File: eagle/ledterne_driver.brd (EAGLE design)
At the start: 24.3 x 23.1 mm, 9 parts, among them IC1 MEGA8-AI

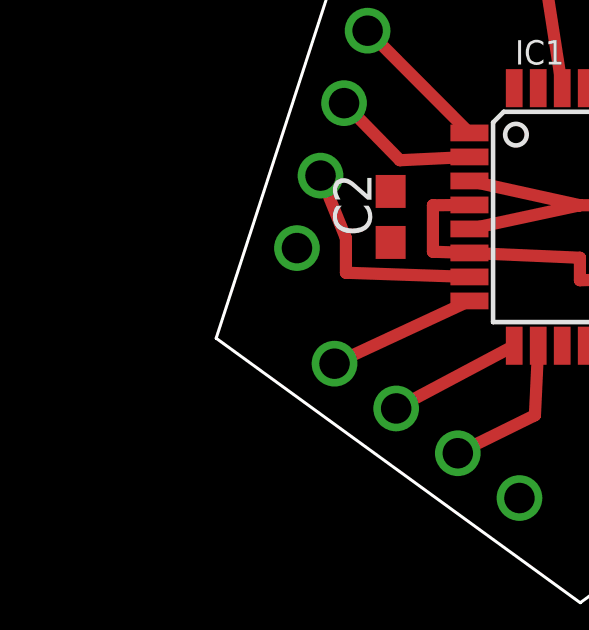
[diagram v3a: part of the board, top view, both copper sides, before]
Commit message: Add connector for supply voltage
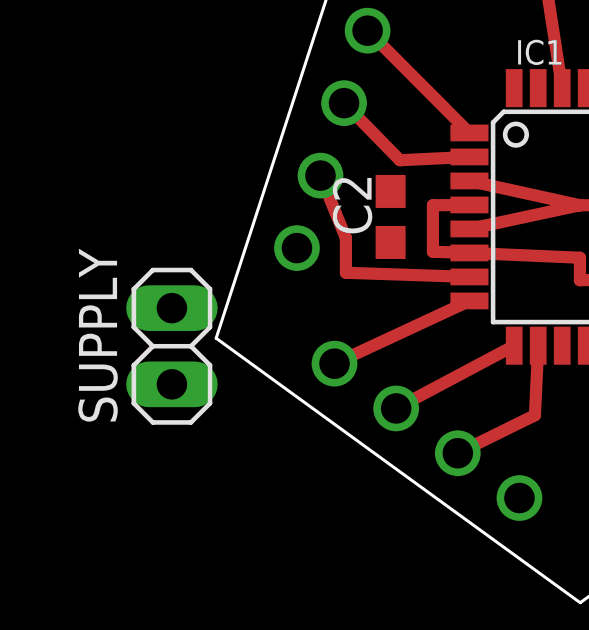
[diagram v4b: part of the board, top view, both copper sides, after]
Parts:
- added SUPPLY: (no value), pinhead:1X02
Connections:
- net GND: now also SUPPLY.2
- net VCC: now also SUPPLY.1
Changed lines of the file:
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@@
 <?xml version="1.0" encoding="utf-8"?>
 <!DOCTYPE eagle SYSTEM "eagle.dtd">
-<eagle version="7.4.0">
+<eagle version="7.3.0">
 <drawing>
 <settings>
@@
 <element name="JP4" library="pinhead_round_pads" package="1X04/90" value="" x="9.162684375" y="6.3972875" rot="MR216"/>
 <element name="JP5" library="pinhead_round_pads" package="1X04/90" value="" x="4.62179375" y="20.3727125" rot="MR288"/>
+<element name="SUPPLY" library="pinhead" package="1X02" value="" x="2.9" y="12.3" rot="R90"/>
 </elements>
 <signals>
@@
 <contactref element="JP4" pad="4"/>
 <contactref element="JP5" pad="4"/>
+<contactref element="SUPPLY" pad="2"/>
 <wire x1="23.33" y1="17.22" x2="23.597328125" y2="22.81888125" width="0" layer="19" extent="1-1"/>
 <wire x1="21.4026" y1="17.01" x2="23.33" y2="17.22" width="0" layer="19" extent="1-1"/>
-<wire x1="29.63" y1="10.38" x2="12.8174" y2="16.21" width="0" layer="19" extent="1-1"/>
-<wire x1="10.19" y1="17.46" x2="29.63" y2="10.38" width="0" layer="19" extent="1-1"/>
+<wire x1="10.19" y1="17.46" x2="12.8174" y2="17.81" width="0" layer="19" extent="1-1"/>
 <wire x1="7.067965625" y1="15.57183125" x2="10.19" y2="17.46" width="0" layer="19" extent="1-1"/>
+<wire x1="2.9" y1="13.57" x2="7.067965625" y2="15.57183125" width="0" layer="19" extent="1-1"/>
 <wire x1="24.700209375" y1="11.719103125" x2="23.33" y2="17.22" width="0" layer="19" extent="1-1"/>
+<wire x1="29.63" y1="10.38" x2="24.700209375" y2="11.719103125" width="0" layer="19" extent="1-1"/>
 <wire x1="12.7" y1="25.2" x2="12.8174" y2="17.81" width="0" layer="19" extent="1-1"/>
 <wire x1="14.484503125" y1="7.240178125" x2="12.8174" y2="16.21" width="0" layer="19" extent="1-1"/>
@@
 <wire x1="11.6" y1="17" x2="11.6" y2="15.45" width="0.4064" layer="1"/>
 <wire x1="11.6" y1="15.45" x2="12.8174" y2="15.41" width="0.4064" layer="1"/>
+<contactref element="SUPPLY" pad="1"/>
 <wire x1="21.4026" y1="14.61" x2="42.33" y2="10.38" width="0" layer="19" extent="1-1"/>
 <wire x1="10.19" y1="15.76" x2="11.6" y2="15.45" width="0" layer="19" extent="1-1"/>
+<wire x1="2.9" y1="11.03" x2="10.19" y2="15.76" width="0" layer="19" extent="1-1"/>
 </signal>
 <signal name="RESET">
 <contactref element="IC1" pad="29"/>
 <contactref element="ISP" pad="5"/>
-<wire x1="39.79" y1="10.38" x2="16.71" y2="20.9026" width="0" layer="19" extent="1-1"/>
+<wire x1="16.71" y1="20.9026" x2="39.79" y2="10.38" width="0" layer="19" extent="1-1"/>
 </signal>
 <signal name="MOSI">
@@
 <wire x1="19.1" y1="11.1" x2="19.11" y2="12.3174" width="0.4064" layer="1"/>
 <contactref element="JP3" pad="2"/>
-<wire x1="19.11" y1="12.3174" x2="37.25" y2="10.38" width="0" layer="19" extent="1-1"/>
+<wire x1="20.590403125" y1="8.733153125" x2="37.25" y2="10.38" width="0" layer="19" extent="1-1"/>
 </signal>
 <signal name="MISO">
@@
 <wire x1="19.95" y1="11.95" x2="19.91" y2="12.3174" width="0.4064" layer="1"/>
 <contactref element="JP3" pad="3"/>
-<wire x1="19.91" y1="12.3174" x2="34.71" y2="10.38" width="0" layer="19" extent="1-1"/>
+<wire x1="22.64530625" y1="10.226128125" x2="34.71" y2="10.38" width="0" layer="19" extent="1-1"/>
 </signal>
 <signal name="SCK">
@@
 <wire x1="23.495" y1="13.97" x2="25.9520375" y2="15.57183125" width="0.4064" layer="1"/>
 <contactref element="JP2" pad="1"/>
-<wire x1="32.17" y1="10.38" x2="21.4026" y2="13.81" width="0" layer="19" extent="1-1"/>
+<wire x1="25.9520375" y1="15.57183125" x2="32.17" y2="10.38" width="0" layer="19" extent="1-1"/>
 </signal>
 <signal name="N$1">
